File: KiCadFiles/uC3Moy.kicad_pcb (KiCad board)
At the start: 2 copper layers, 36.1 x 49.7 mm, 25 parts, among them J1 JACK, J2 JACK_INT, P1 CONN_2, U1 OPA2132, U2 TLE2426, U3 TLE2426

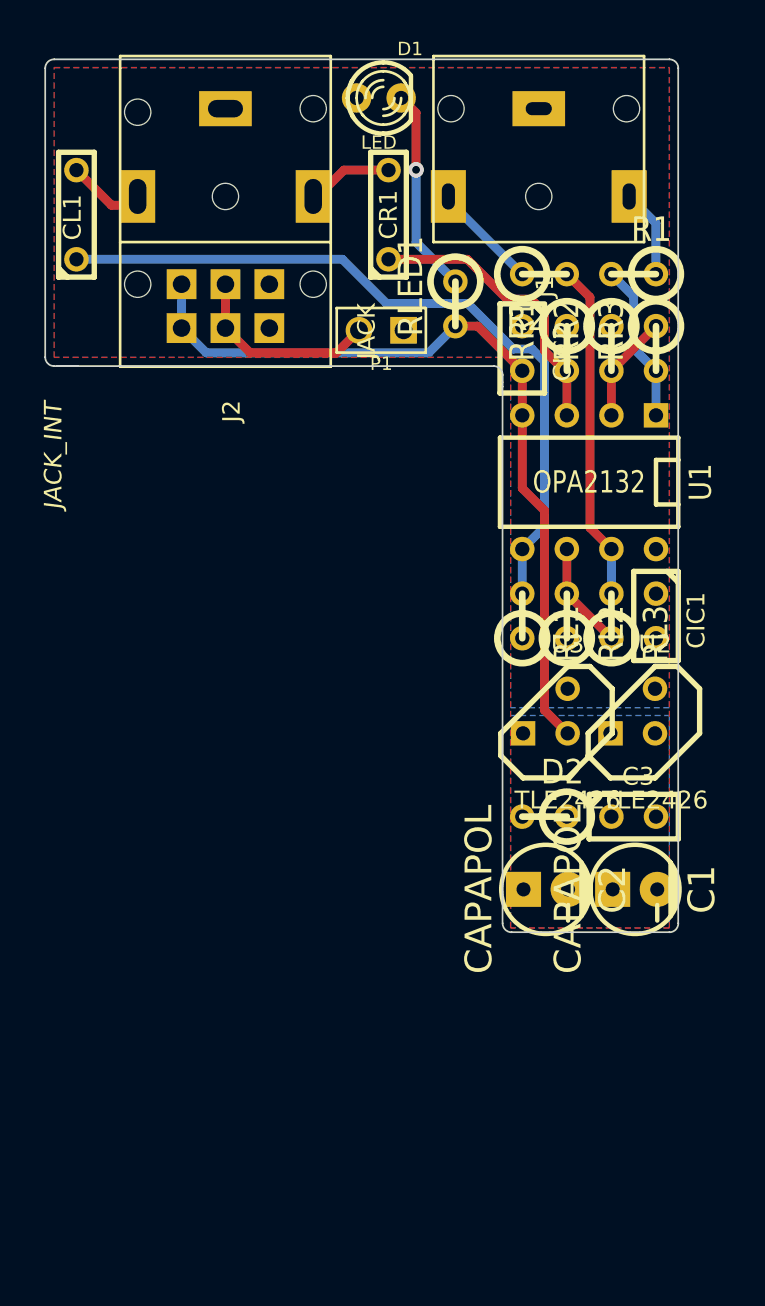
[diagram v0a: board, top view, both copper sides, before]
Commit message: Modified lenght to fit under 50x50mm boards
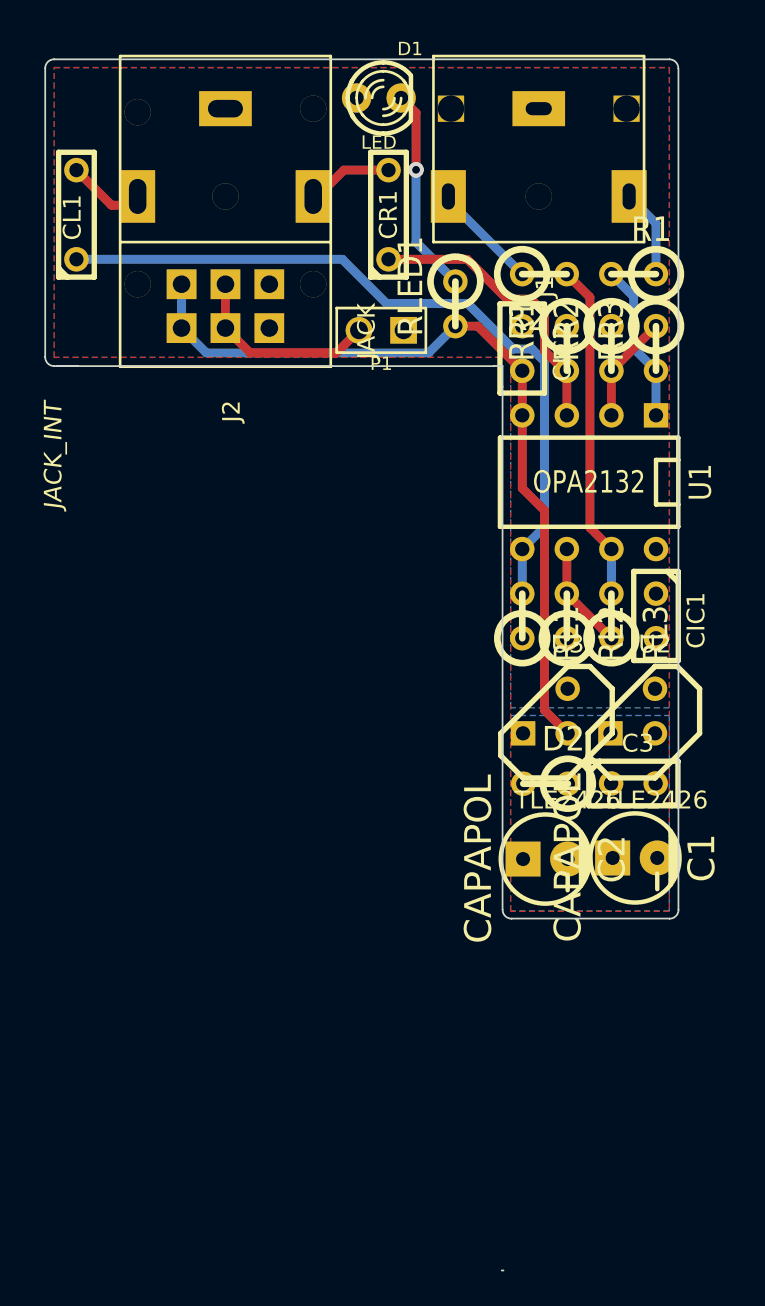
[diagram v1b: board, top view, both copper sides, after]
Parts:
- removed G***: LOGO, LOGO
- moved C3 1.89 mm to (241.6, 167.2)
- moved D2 1.88 mm to (236.6, 167.2)
- moved C1 1.79 mm to (241.7, 171.4)
- moved C2 1.73 mm to (236.6, 171.5)
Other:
- board size 36.1 x 49.7 mm -> 36.1 x 69 mm

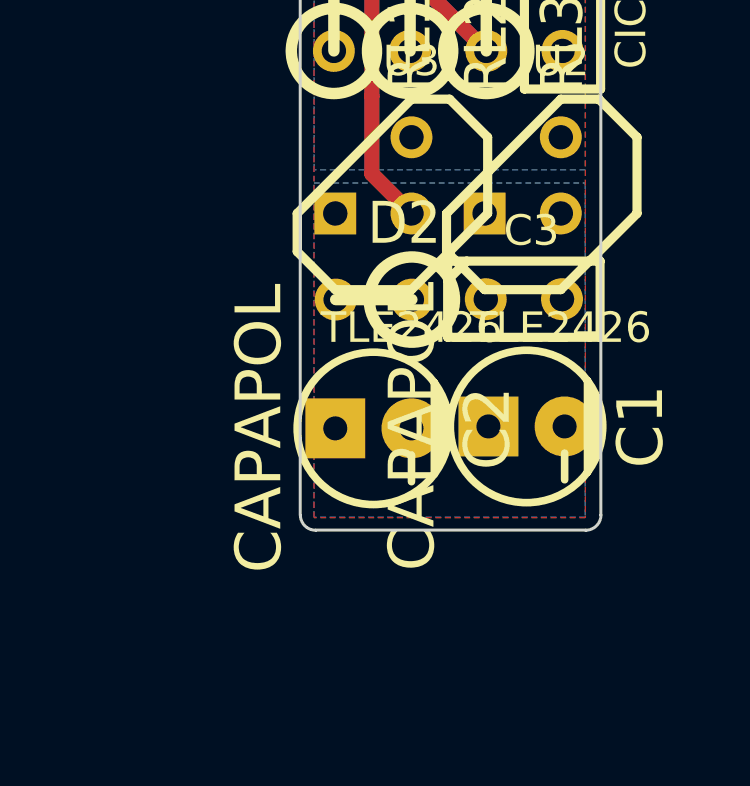
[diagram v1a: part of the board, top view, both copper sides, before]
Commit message: Silkscreen upgrades
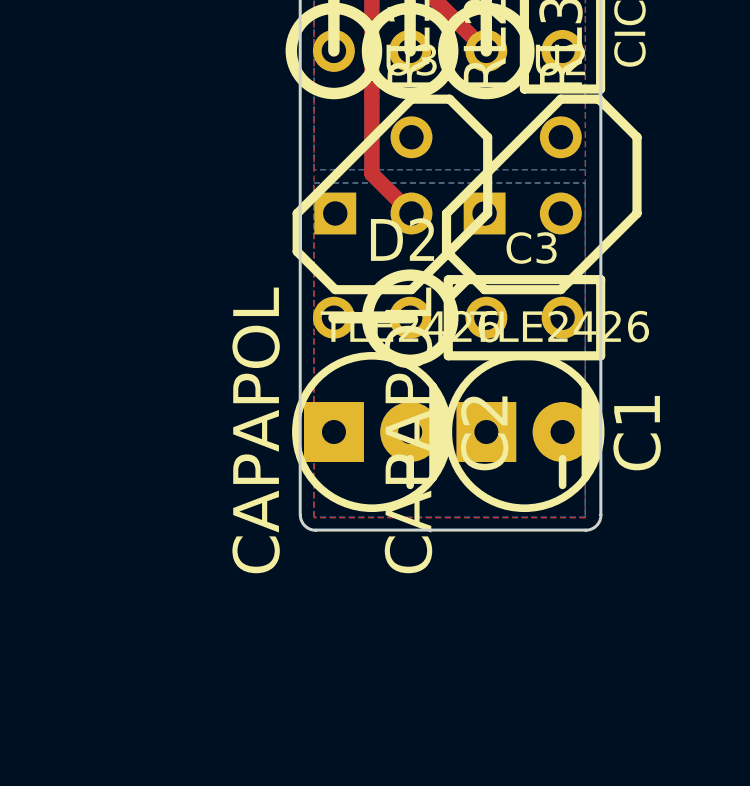
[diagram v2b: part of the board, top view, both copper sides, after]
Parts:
- moved C3 0.62 mm to (241.6, 167.8)
- moved D2 0.61 mm to (236.5, 167.8)
- moved C1 0.20 mm to (241.6, 171.6)
- moved C2 0.13 mm to (236.5, 171.6)
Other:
- board text added: "uC3Moy"
- board text added: "v1.0"
- board text removed: "V0.1"
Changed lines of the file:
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@@
     (links 47)
     (no_connects 0)
-    (area 207.711 124.66655 247.130711 194.990001)
+    (area 208.031199 125.888099 244.211901 194.990001)
     (thickness 1.6)
-    (drawings 19)
+    (drawings 20)
     (tracks 59)
     (zones 0)
@@
     (pad_drill 0.8128)
     (pad_to_mask_clearance 0)
-    (aux_axis_origin 240.3348 143.68018)
-    (visible_elements 7FFFFFFF)
+    (aux_axis_origin 240.34242 143.68272)
+    (visible_elements 7FFE3FFF)
     (pcbplotparams
       (layerselection 284196865)
@@
       (drillshape 0)
       (scaleselection 1)
-      (outputdirectory gerber/))
+      (outputdirectory /home/jorfru/uC3Moy/gerber/))
   )
   (net 0 "")
@@
   )
   (module C1 (layer F.Cu)
-    (at 241.5921 167.1955)
+    (at 241.61242 167.81272)
     (descr "Condensateur e = 1 pas")
     (tags C)
@@
   )
   (module CP_5x11mm (layer F.Cu)
-    (at 241.681 171.4373 270)
+    (at 241.61242 171.62272 270)
     (descr "Capacitor, pol, cyl 5x11mm")
     (fp_text reference C1 (at 0 -3.81 270) (layer F.SilkS)
@@
   )
   (module CP_5x11mm (layer F.Cu)
-    (at 236.5756 171.5008 270)
+    (at 236.53242 171.62272 270)
     (descr "Capacitor, pol, cyl 5x11mm")
     (fp_text reference C2 (at 0 -3.81 270) (layer F.SilkS)
@@
   )
   (module R1 (layer F.Cu)
-    (at 236.5883 167.2082 180)
+    (at 236.53242 167.81272 180)
     (descr "Resistance verticale")
     (tags R)
@@
       (rotate (xyz 0 0 0))
     )
+  )
+  (gr_text v1.0 (at 211.64042 141.46022) (layer B.SilkS)
+    (effects (font (size 1.5 1.5) (thickness 0.3)) (justify mirror))
   )
   (gr_line (start 244.1575 174.3837) (end 244.1575 126.4666) (angle 90) (layer Edge.Cuts) (width 0.1))
@@
     (effects (font (size 4 3.5) (thickness 0.8)) (justify mirror))
   )
-  (gr_text V0.1 (at 211.8 141.1) (layer B.SilkS)
-    (effects (font (size 1.5 1.5) (thickness 0.3)) (justify mirror))
+  (gr_text uC3Moy (at 227.26142 138.92022) (layer B.SilkS)
+    (effects (font (size 1 1) (thickness 0.25)) (justify mirror))
   )
   (gr_line (start 234.19 194.94) (end 234.09 194.94) (angle 90) (layer Edge.Cuts) (width 0.1))

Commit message: guitar logo added to back silkscreen
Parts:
- added G***: LOGO, LOGO, B.Cu at (239.6, 158.8)
